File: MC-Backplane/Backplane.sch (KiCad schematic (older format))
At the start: 1 part

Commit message: beginning layout
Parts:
- J1: renamed from J?; value Barrel_Jack -> 1730010; footprint (none) -> Footprints_MC-Backplane:1730010; symbol Connector:Barrel_Jack -> Existing_IC_Models:1730010
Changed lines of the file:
@@
 $EndDescr
 $Comp
-L Connector:Barrel_Jack J?
+L Existing_IC_Models:1730010 J1
 U 1 1 61F21CB0
-P 3950 7150
-F 0 "J?" H 4007 7475 50  0000 C CNN
-F 1 "Barrel_Jack" H 4007 7384 50  0000 C CNN
-F 2 "" H 4000 7110 50  0001 C CNN
-F 3 "~" H 4000 7110 50  0001 C CNN
-	1    3950 7150
-	1    0    0    -1
+P 4250 7150
+F 0 "J1" H 4650 7425 50  0000 C CNN
+F 1 "1730010" H 4625 7325 50  0000 C CNN
+F 2 "Footprints_MC-Backplane:1730010" H 4300 7110 50  0001 C CNN
+F 3 "https://www.digikey.com/en/products/detail/phoenix-contact/1730010/2511110" H 4300 7110 50  0001 C CNN
+	1    4250 7150
+	-1   0    0    1
 $EndComp
 Text GLabel 1550 725  0    50   Input ~ 0
 24V
-Text GLabel 8800 700  0    50   Input ~ 0
+Text GLabel 8800 1025 0    50   Input ~ 0
 24V
 Text GLabel 8550 3650 0    50   Input ~ 0
@@
 Text GLabel 1575 3750 0    50   Input ~ 0
 24V
-Text GLabel 5550 7050 2    50   Input ~ 0
+Text GLabel 5550 7050 2    50   Output ~ 0
 24V
 Text Notes 1000 1450 0    50   ~ 0
@@
 slot 10-13
 Wire Wire Line
-	4250 7250 4350 7250
-$Sheet
-S 8800 600  1150 2625
-U 61E8CB73
-F0 "DeltaSigmaSlots" 50
-F1 "DeltaSigmasSlots.sch" 50
-F2 "24V" I L 8800 700 50
-F3 "SD1_D1" I L 8800 1550 50
-F4 "SD1_C1" I L 8800 1625 50
-F5 "SD1_D2" I L 8800 1700 50
-F6 "SD1_C2" I L 8800 1775 50
-F7 "SD2_D1" I L 8800 2425 50
-F8 "SD2_C1" I L 8800 2500 50
-F9 "SD1_D3" O L 8800 1850 50
-F10 "SD1_C3" O L 8800 1925 50
-F11 "SD1_D4" O L 8800 2000 50
-F12 "SD1_C4" O L 8800 2075 50
-F13 "SD2_D3" O L 8800 2725 50
-F14 "SD2_C3" O L 8800 2800 50
-F15 "SD2_D4" O L 8800 2875 50
-F16 "SD2_C4" O L 8800 2950 50
-F17 "CLOCK" I R 9950 725 50
-F18 "GND" I R 9950 2050 50
-F19 "SD2_D2" I L 8800 2575 50
-F20 "SD2_C2" I L 8800 2650 50
-F21 "SD1_EPWM14A_CLK_OUT" I L 8800 1400 50
-F22 "SD1_EPWM14B_CLK_OUT" I L 8800 1475 50
-F23 "SD2_EPWM13A_CLK_OUT" I L 8800 2275 50
-F24 "SD2_EPWM13B_CLK_OUT" I L 8800 2350 50
-F25 "GPIO13_SAFE_STATE_FLAG" B R 9950 3050 50
-F26 "GPIO12_EMITTER_ENABLE" I R 9950 3150 50
-$EndSheet
-Wire Wire Line
 	10200 5550 10200 5900
 Wire Wire Line
@@
 	10100 2050 10100 2200
 $Comp
-L power:GND #PWR?
+L power:GND #PWR0101
 U 1 1 6210D719
 P 10100 2200
-F 0 "#PWR?" H 10100 1950 50  0001 C CNN
+F 0 "#PWR0101" H 10100 1950 50  0001 C CNN
 F 1 "GND" H 10105 2027 50  0000 C CNN
 F 2 "" H 10100 2200 50  0001 C CNN
@@
 $EndComp
 $Comp
-L power:GND #PWR?
+L power:GND #PWR0102
 U 1 1 6210DC40
 P 3375 6100
-F 0 "#PWR?" H 3375 5850 50  0001 C CNN
+F 0 "#PWR0102" H 3375 5850 50  0001 C CNN
 F 1 "GND" H 3380 5927 50  0000 C CNN
 F 2 "" H 3375 6100 50  0001 C CNN
@@
 $EndComp
 $Comp
-L power:GND #PWR?
+L power:GND #PWR0103
 U 1 1 6210E3A4
 P 3425 3300
-F 0 "#PWR?" H 3425 3050 50  0001 C CNN
+F 0 "#PWR0103" H 3425 3050 50  0001 C CNN
 F 1 "GND" H 3430 3127 50  0000 C CNN
 F 2 "" H 3425 3300 50  0001 C CNN
 F 3 "" H 3425 3300 50  0001 C CNN
 	1    3425 3300
-	1    0    0    -1
-$EndComp
-$Comp
-L power:GND #PWR?
-U 1 1 6210E750
-P 7200 6000
-F 0 "#PWR?" H 7200 5750 50  0001 C CNN
-F 1 "GND" H 7205 5827 50  0000 C CNN
-F 2 "" H 7200 6000 50  0001 C CNN
-F 3 "" H 7200 6000 50  0001 C CNN
-	1    7200 6000
 	1    0    0    -1
 $EndComp
@@
 slots 4-6
 $Comp
-L power:GND #PWR?
+L power:GND #PWR0105
 U 1 1 62187F54
 P 10200 5900
-F 0 "#PWR?" H 10200 5650 50  0001 C CNN
+F 0 "#PWR0105" H 10200 5650 50  0001 C CNN
 F 1 "GND" H 10205 5727 50  0000 C CNN
 F 2 "" H 10200 5900 50  0001 C CNN
@@
 	1    0    0    -1
 $EndComp
-Wire Wire Line
-	10200 5550 9950 5550
 $Sheet
 S 8550 3550 1375 2150
@@
 Text GLabel 4500 1150 0    50   Output ~ 0
 CLOCK
-Text GLabel 9950 725  2    50   Input ~ 0
+Text GLabel 9950 1025 2    50   Input ~ 0
 CLOCK
 Text GLabel 9925 3850 2    50   Input ~ 0
@@
 CLOCK
 $Comp
-L power:GND #PWR?
+L power:GND #PWR0106
 U 1 1 62468E19
 P 4350 7450
-F 0 "#PWR?" H 4350 7200 50  0001 C CNN
+F 0 "#PWR0106" H 4350 7200 50  0001 C CNN
 F 1 "GND" H 4355 7277 50  0000 C CNN
 F 2 "" H 4350 7450 50  0001 C CNN
@@
 $EndComp
 Wire Wire Line
-	4350 7250 4350 7450
-Wire Wire Line
 	5550 7300 5950 7300
 $Comp
-L power:GND #PWR?
+L power:GND #PWR0107
 U 1 1 62E04A60
 P 5950 7500
-F 0 "#PWR?" H 5950 7250 50  0001 C CNN
+F 0 "#PWR0107" H 5950 7250 50  0001 C CNN
 F 1 "GND" H 5955 7327 50  0000 C CNN
 F 2 "" H 5950 7500 50  0001 C CNN
@@
 Wire Wire Line
 	5950 7300 5950 7500
+$Sheet
+S 8800 600  1150 2625
+U 61E8CB73
+F0 "DeltaSigmaSlots" 50
+F1 "DeltaSigmasSlots.sch" 50
+F2 "24V" I L 8800 1025 50
+F3 "SD1_D1" I L 8800 1550 50
+F4 "SD1_C1" I L 8800 1625 50
+F5 "SD1_D2" I L 8800 1700 50
+F6 "SD1_C2" I L 8800 1775 50
+F7 "SD2_D1" I L 8800 2425 50
+F8 "SD2_C1" I L 8800 2500 50
+F9 "SD1_D3" O L 8800 1850 50
+F10 "SD1_C3" O L 8800 1925 50
+F11 "SD1_D4" O L 8800 2000 50
+F12 "SD1_C4" O L 8800 2075 50
+F13 "SD2_D3" O L 8800 2725 50
+F14 "SD2_C3" O L 8800 2800 50
+F15 "SD2_D4" O L 8800 2875 50
+F16 "SD2_C4" O L 8800 2950 50
+F17 "CLOCK" I R 9950 1025 50
+F18 "GND" I R 9950 2050 50
+F19 "SD2_D2" I L 8800 2575 50
+F20 "SD2_C2" I L 8800 2650 50
+F21 "SD1_EPWM14A_CLK_OUT" I L 8800 1400 50
+F22 "SD1_EPWM14B_CLK_OUT" I L 8800 1475 50
+F23 "SD2_EPWM13A_CLK_OUT" I L 8800 2275 50
+F24 "SD2_EPWM13B_CLK_OUT" I L 8800 2350 50
+F25 "GPIO13_SAFE_STATE_FLAG" B R 9950 3050 50
+F26 "GPIO12_EMITTER_ENABLE" I R 9950 3150 50
+$EndSheet
+Wire Wire Line
+	4250 7150 4350 7150
+Wire Wire Line
+	9925 5550 10200 5550
+Wire Wire Line
+	4350 7150 4350 7450
+$Comp
+L power:GND #PWR0104
+U 1 1 62FA57FB
+P 7200 6000
+F 0 "#PWR0104" H 7200 5750 50  0001 C CNN
+F 1 "GND" H 7205 5827 50  0000 C CNN
+F 2 "" H 7200 6000 50  0001 C CNN
+F 3 "" H 7200 6000 50  0001 C CNN
+	1    7200 6000
+	1    0    0    -1
+$EndComp
 $EndSCHEMATC

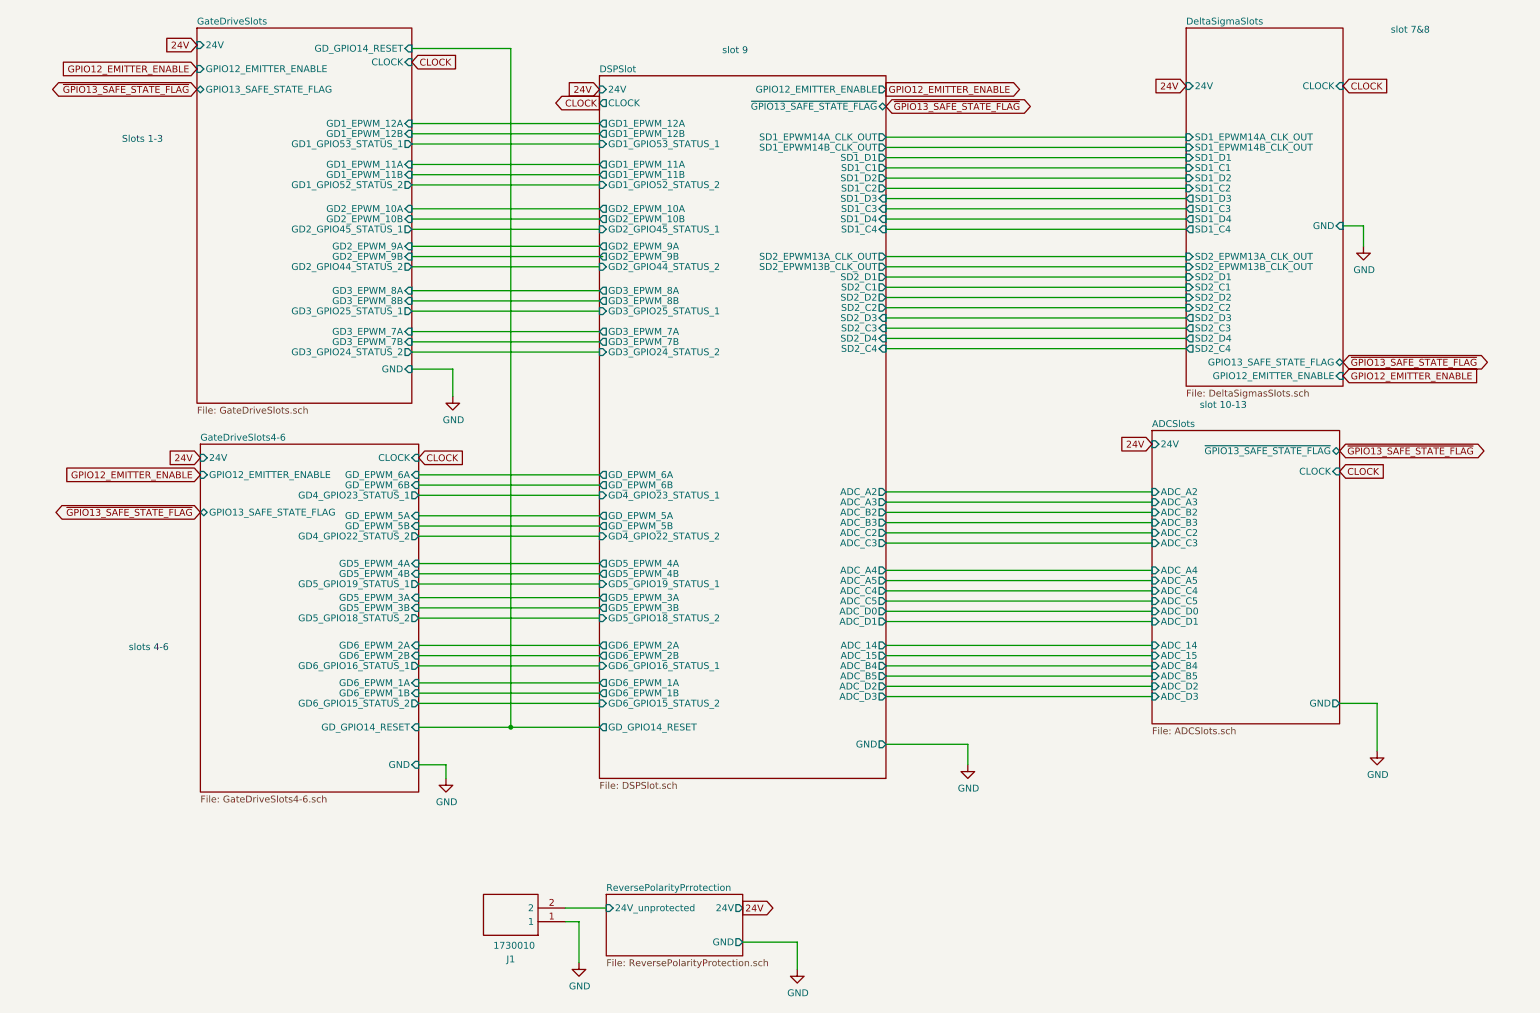
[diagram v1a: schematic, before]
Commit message: schematic reorg and layout begins
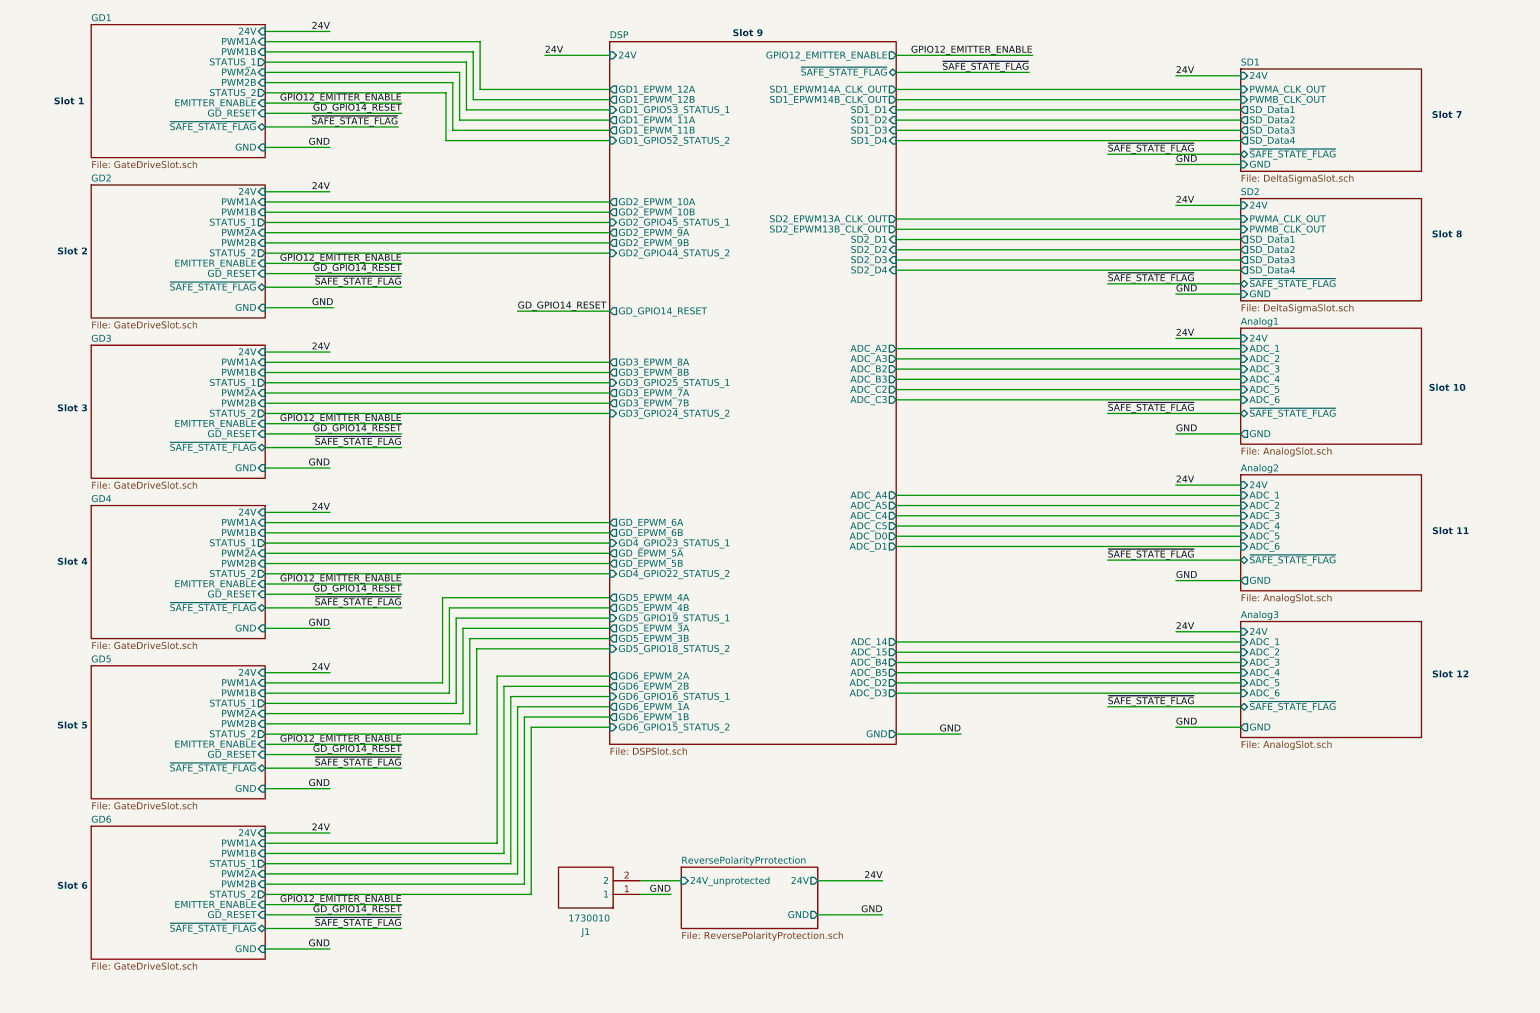
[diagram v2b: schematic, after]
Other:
- note added: "Slot 1"
- note added: "Slot 10"
- note added: "Slot 11"
- note added: "Slot 12"
- note added: "Slot 2\n"
- note added: "Slot 3\n"
- note added: "Slot 4\n"
- note added: "Slot 5\n"
- note added: "Slot 6\n"
- note added: "Slot 7"
- note added: "Slot 8"
- note added: "Slot 9"
- note removed: "Slots 1-3"
- note removed: "slot 10-13"
- note removed: "slot 7&8"
- note removed: "slot 9"
- note removed: "slots 4-6"
- moved on the sheet: J1

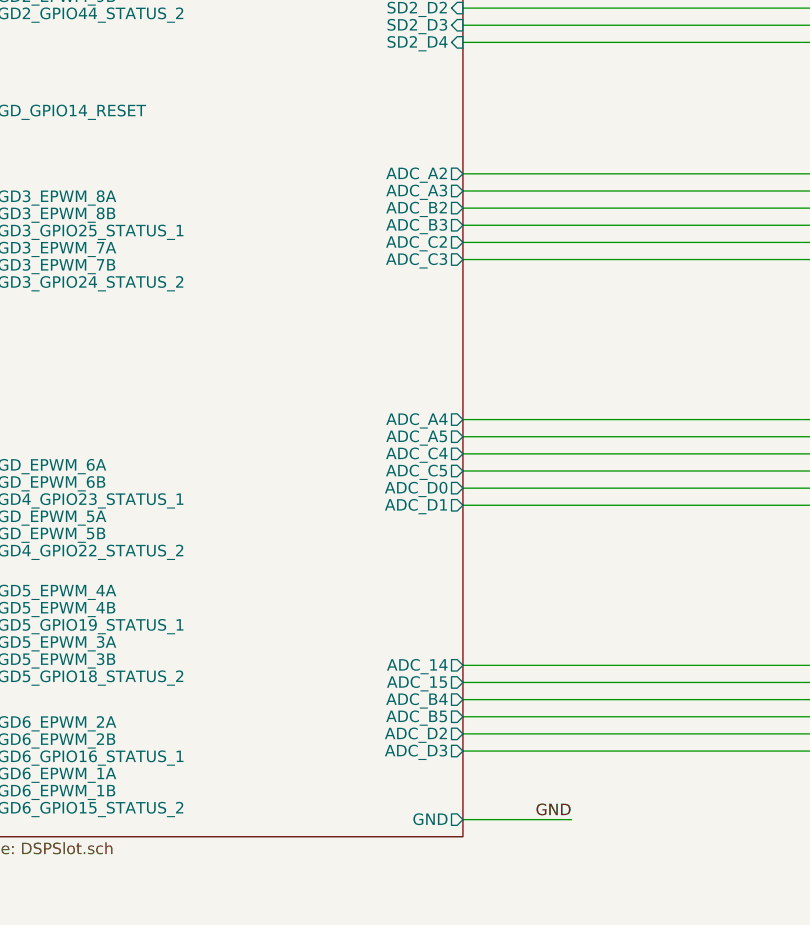
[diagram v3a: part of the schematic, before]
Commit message: layout done: cleaning up and checking MH
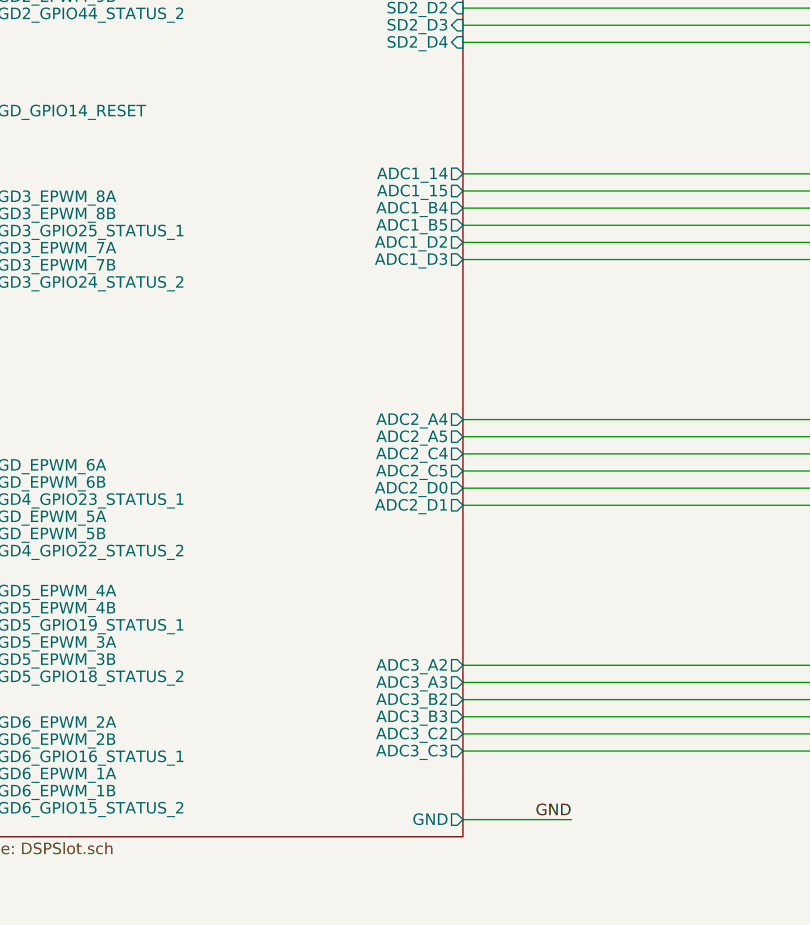
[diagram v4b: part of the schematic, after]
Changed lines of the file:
@@
 F2 "24V" I L 4575 800 50
 F3 "GND" O R 6675 5775 50
-F4 "ADC_A2" O R 6675 2950 50
-F5 "ADC_A3" O R 6675 3025 50
-F6 "ADC_A4" O R 6675 4025 50
-F7 "ADC_A5" O R 6675 4100 50
-F8 "ADC_B2" O R 6675 3100 50
-F9 "ADC_B3" O R 6675 3175 50
-F10 "ADC_C2" O R 6675 3250 50
-F11 "ADC_C3" O R 6675 3325 50
-F12 "ADC_C4" O R 6675 4175 50
-F13 "ADC_C5" O R 6675 4250 50
-F14 "ADC_B4" O R 6675 5250 50
-F15 "ADC_B5" O R 6675 5325 50
-F16 "ADC_D2" O R 6675 5400 50
-F17 "ADC_D3" O R 6675 5475 50
+F4 "ADC3_A2" O R 6675 5100 50
+F5 "ADC3_A3" O R 6675 5175 50
+F6 "ADC2_A4" O R 6675 4025 50
+F7 "ADC2_A5" O R 6675 4100 50
+F8 "ADC3_B2" O R 6675 5250 50
+F9 "ADC3_B3" O R 6675 5325 50
+F10 "ADC3_C2" O R 6675 5400 50
+F11 "ADC3_C3" O R 6675 5475 50
+F12 "ADC2_C4" O R 6675 4175 50
+F13 "ADC2_C5" O R 6675 4250 50
+F14 "ADC1_B4" O R 6675 3100 50
+F15 "ADC1_B5" O R 6675 3175 50
+F16 "ADC1_D2" O R 6675 3250 50
+F17 "ADC1_D3" O R 6675 3325 50
 F18 "SD2_EPWM13A_CLK_OUT" O R 6675 2000 50
 F19 "SD2_EPWM13B_CLK_OUT" O R 6675 2075 50
@@
 F59 "GD2_EPWM_10A" O L 4575 1875 50
 F60 "GD2_EPWM_10B" O L 4575 1950 50
-F61 "ADC_D0" O R 6675 4325 50
-F62 "ADC_D1" O R 6675 4400 50
-F63 "ADC_14" O R 6675 5100 50
-F64 "ADC_15" O R 6675 5175 50
+F61 "ADC2_D0" O R 6675 4325 50
+F62 "ADC2_D1" O R 6675 4400 50
+F63 "ADC1_14" O R 6675 2950 50
+F64 "ADC1_15" O R 6675 3025 50
 F65 "SD1_D1" I R 6675 1200 50
 F66 "SD1_D4" I R 6675 1425 50
